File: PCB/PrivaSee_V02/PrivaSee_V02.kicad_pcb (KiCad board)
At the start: 4 copper layers, 73.8 x 90 mm, 33 parts, among them J1 RFPC-SMA27-F, J2 Batt_Solder_Point, J3 Conn_02x06_Odd_Even, J4 VOUT_TEST, J5 GND_TEST, J6 IR_TEST, J7 RF_TEST, SW1 Switch, SW2 SW_Push, U2 LM358, U3 254, U4 DFR0568, U6 ESP32-C5-DevKitC-1

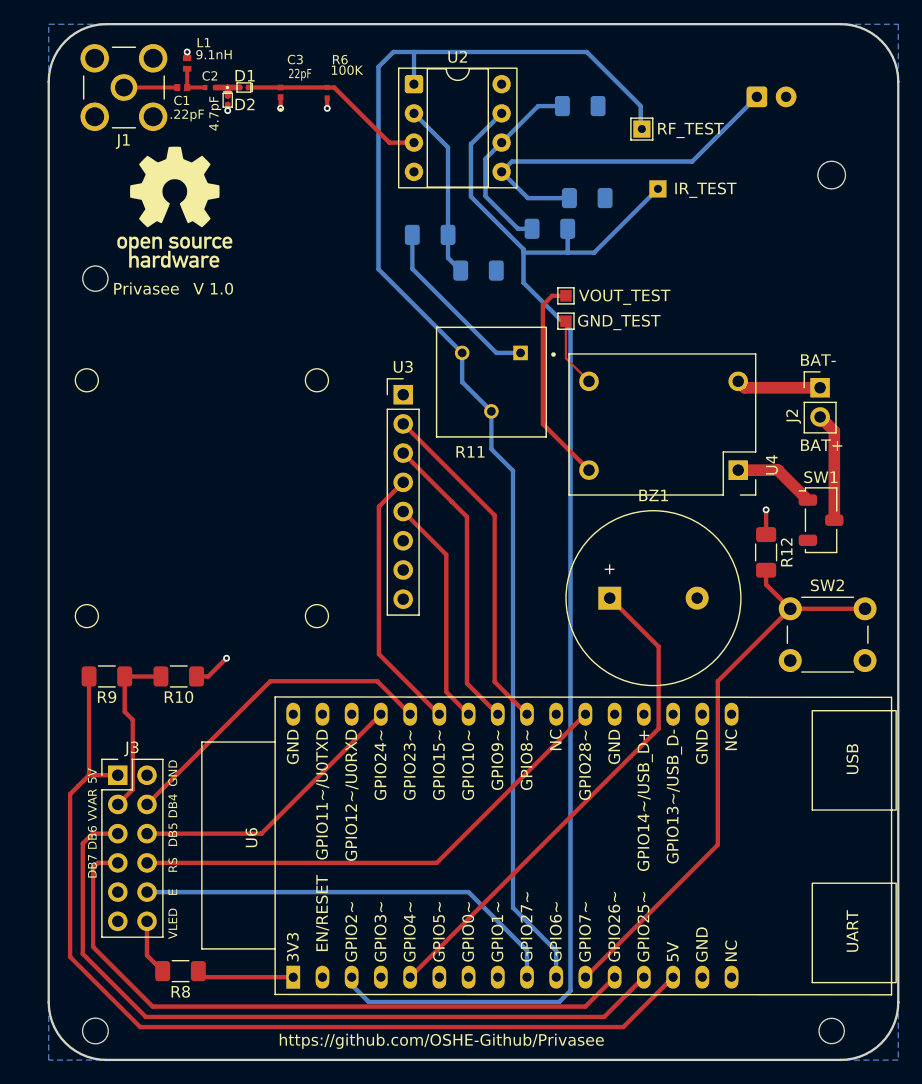
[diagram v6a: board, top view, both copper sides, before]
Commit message: more tracing/changes
teardrops added for signal pin. Screw mounts adjusted to 1.7mm. Sd breakout adjusted.
In-progress
-Button needs to be changed to match footprint. Lab buttons still work
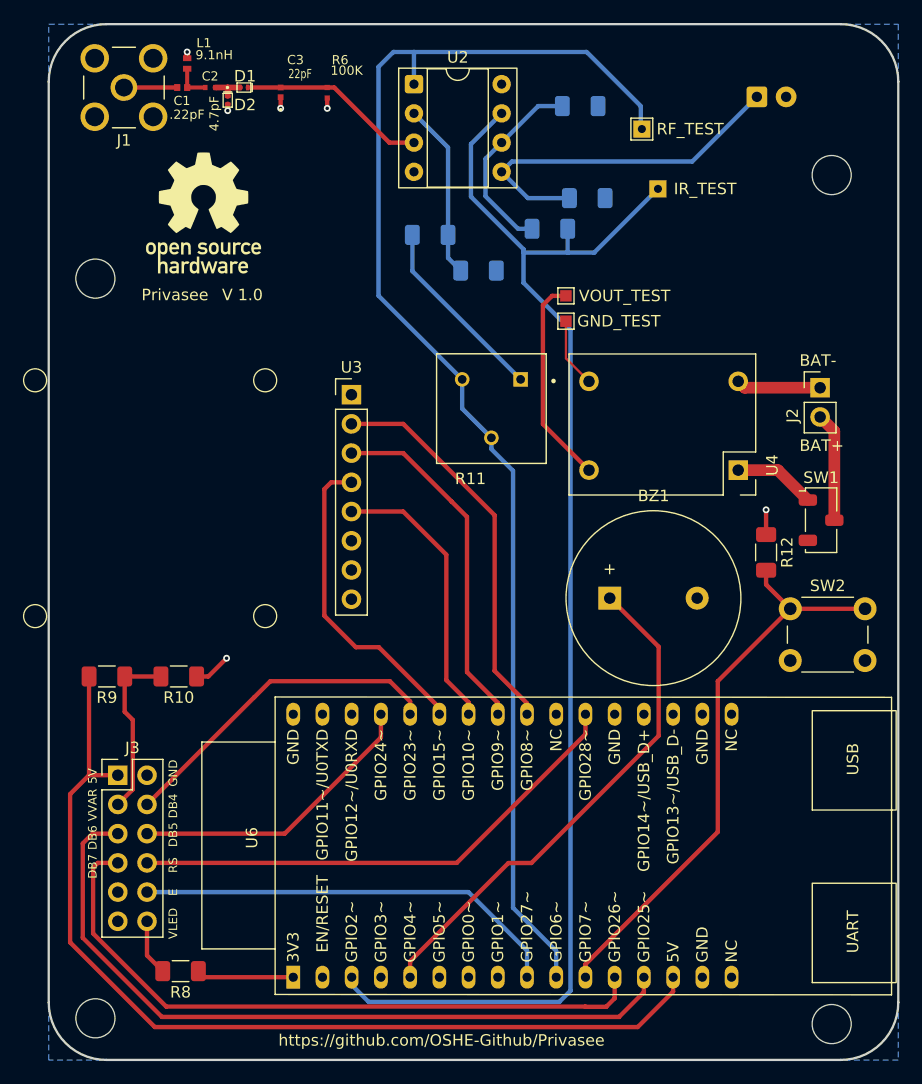
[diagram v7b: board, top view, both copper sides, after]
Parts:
- moved U3 4.50 mm to (92.4, 53.8)
- moved ? 2.55 mm to (79.5, 38.0)
- moved R11 2.30 mm to (104.5, 55.0)
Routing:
- net Net-(U3-DI): track 26.1 -> 30.6 mm
- net Net-(U3-CS): track 29.7 -> 34.2 mm
- net Net-(U3-CLK): track 20.0 -> 24.5 mm
- net Net-(U3-DO): track 23.2 -> 27.5 mm
- net LCD_DB5: track 24.6 -> 25.8 mm
- net Net-(BZ1-+): track 44.0 -> 45.2 mm
- net Net-(R1-Pad1): track 15.4 -> 16.5 mm
- net LCD_RS: track 43.5 -> 44.5 mm
- net LCD_DB4: track 28.5 -> 29.1 mm
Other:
- outline, holes or cut-outs redrawn

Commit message: capacitor replacement
handsolderable foot print
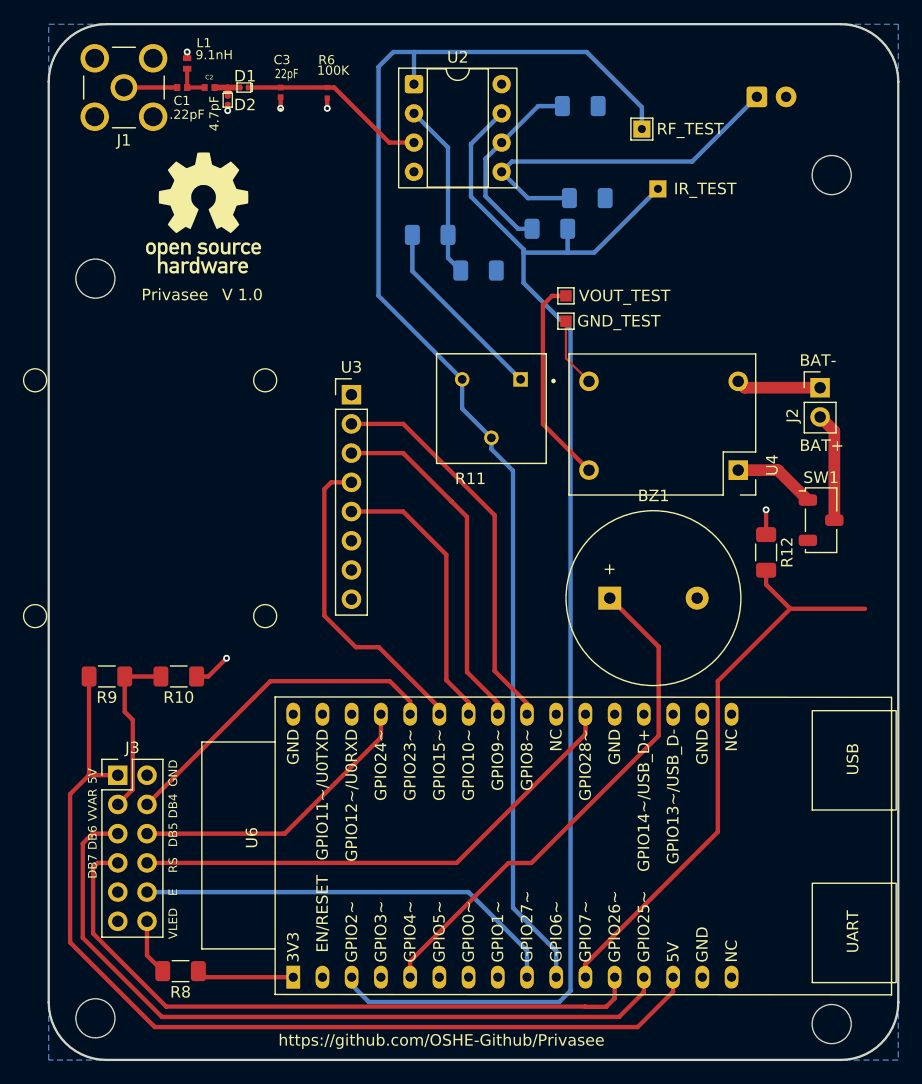
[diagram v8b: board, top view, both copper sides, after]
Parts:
- removed SW2: SW_Push, Button_Switch_THT:SW_PUSH_6mm_H4.3mm
- C2: value GJM1555C1H4R7CB01D -> GJM1555C1H4R7BB01D; footprint Snapeda:G-155_MUR-L -> Snapeda:CAPC1005X55N
- moved C2 0.06 mm to (80.0, 27.1)
